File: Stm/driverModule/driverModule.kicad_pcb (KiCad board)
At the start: 4 copper layers, 111.9 x 61.1 mm, 62 parts, among them J1 1723104104, J2 2041119-1 (Mini Pcie Express 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, J3 1723103105, J4 353180420, J5 1723103105, Q1 BSS138, Q2 BSS138, Q3 AON7410, U1 TLE94103EP, U102 ADM7171ACPZ-3.0-R7, U103 TJA1051T-3, U104 TPS5410DR, U2 74LVC2G04, U201 DRV8838, U204 VNH5019A-E, U3 MCP2003B-E/SN

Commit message: routing
Finished PCB routing
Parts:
- added 12V: TestPoint_Small, TestPoint:TestPoint_Pad_1.0x1.0mm, F.Cu at (183.0, 111.6)
- added 3V3: TestPoint_Small, TestPoint:TestPoint_Pad_1.0x1.0mm, F.Cu at (210.7, 64.8)
- added 5V: TestPoint_Small, TestPoint:TestPoint_Pad_1.0x1.0mm, F.Cu at (206.5, 91.2)
- added MISO: TestPoint_Small, TestPoint:TestPoint_Pad_1.0x1.0mm, F.Cu at (149.1, 75.6)
- added MOSI: TestPoint_Small, TestPoint:TestPoint_Pad_1.0x1.0mm, F.Cu at (146.9, 75.6)
- added cs: TestPoint_Small, TestPoint:TestPoint_Pad_1.0x1.0mm, F.Cu at (151.5, 75.6)
- added sck: TestPoint_Small, TestPoint:TestPoint_Pad_1.0x1.0mm, F.Cu at (161.1, 82.8)
- moved J4 22.0 mm to (200.5, 79.7), turned to 90 degrees
- moved R3 14.3 mm to (168.7, 79.0)
- moved Q2 14.3 mm to (171.4, 79.0)
- moved R4 14.3 mm to (174.4, 79.6)
- moved C102 14.0 mm to (206.1, 101.0), turned to 180 degrees
- moved C103 13.9 mm to (208.7, 101.0)
- moved C106 13.8 mm to (185.2, 108.3), turned to 90 degrees
- moved C101 13.6 mm to (207.0, 94.6)
- moved U102 13.6 mm to (207.2, 97.7)
- moved Q1 13.0 mm to (171.5, 85.0)
- moved R1 13.0 mm to (168.7, 84.9)
- moved R101 12.8 mm to (186.1, 96.3)
- moved U104 12.8 mm to (187.0, 101.9)
- moved C104 12.8 mm to (190.9, 107.3)
- moved C105 12.8 mm to (189.1, 93.2)
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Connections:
- J2 pad 1: /CPU Board Connector/+5V -> +5V
- J2 pad 3: /CPU Board Connector/+5V -> +5V
- J2 pad 5: /CPU Board Connector/+5V -> +5V
- J3 pad 4: /Harness/LatchMotorB -> /Harness/LatchMotorA
- J3 pad 5: /Harness/LatchMotorA -> /Harness/LatchMotorB
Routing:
- net +12V: track 0.00 -> 252.2 mm, vias 0 -> 11
- net +5V: track 0.00 -> 163.1 mm, vias 0 -> 2
- net /Harness/WindowMotorB: track 0.00 -> 91.2 mm, vias 0 -> 2
- net /LatchSensorGreenConnector: track 0.00 -> 77.6 mm
- net /LatchSensorPurpleConnector: track 0.00 -> 72.4 mm
- net /Harness/WindowMotorA: track 0.00 -> 64.5 mm, vias 0 -> 2
- net /LatchPositionThroughSignal: track 0.00 -> 56.1 mm, vias 0 -> 2
- net GND: track 0.00 -> 49.3 mm, vias 0 -> 47
- net /Harness/MirrorMotorXYB: track 0.00 -> 46.3 mm
- net /WindowMotorEnable: track 0.00 -> 44.8 mm, vias 0 -> 3
- net +3V3: track 0.00 -> 42.3 mm, vias 0 -> 11
- net /KeyfobClose3v3: track 0.00 -> 42.3 mm, vias 0 -> 2
- net /Harness/MirrorMotorXA: track 0.00 -> 40.5 mm
- net /CAN_RX: track 0.00 -> 40.0 mm, vias 0 -> 2
- net /Harness/keyFobOpen12V: track 0.00 -> 37.0 mm
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- added copper zone on B.Cu, net +12V
- added copper zone on F.Cu, net +12V
- added copper zone on In2.Cu, net +3V3
- added copper zone on F.Cu, net +5V
- added copper zone on F.Cu, net /Motors Interface/Vout
- added copper zone on F.Cu, net /Power/PH
- added copper zone on F.Cu, net GND
- added copper zone on In1.Cu, net GND
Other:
- board size 111.9 x 61.1 mm -> 100.6 x 64.1 mm

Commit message: routing
Update board routing
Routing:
- net +5V: track 163.1 -> 158.7 mm
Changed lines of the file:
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@@
 		(attr smd)
 		(fp_line
+			(start 14.96 -26.81)
+			(end 14.96 -4.2291)
+			(stroke
+				(width 0.1)
+				(type default)
+			)
+			(layer "F.SilkS")
+		)
+		(fp_line
+			(start -15.04 -26.81)
+			(end 14.96 -26.81)
+			(stroke
+				(width 0.1)
+				(type default)
+			)
+			(layer "F.SilkS")
+		)
+		(fp_line
 			(start 15.0749 -4.2291)
 			(end 10.862937 -4.2291)
@@
 		)
 		(fp_line
+			(start -15.04 0)
+			(end -15.04 -26.81)
+			(stroke
+				(width 0.1)
+				(type default)
+			)
+			(layer "F.SilkS")
+		)
+		(fp_line
 			(start 15.0749 1.46846)
 			(end 15.0749 -4.2291)
@@
 			(layer "B.SilkS")
 		)
+		(fp_circle
+			(center 12.1 -23.88)
+			(end 13.4 -23.88)
+			(stroke
+				(width 0.1)
+				(type solid)
+			)
+			(fill no)
+			(layer "Edge.Cuts")
+		)
+		(fp_circle
+			(center -12.1 -23.88)
+			(end -10.8 -23.88)
+			(stroke
+				(width 0.1)
+				(type solid)
+			)
+			(fill no)
+			(layer "Edge.Cuts")
+		)
 		(fp_line
 			(start 16.580396 -5.408201)
@@
 		(model "${KICAD_USER_3D_MODELS_DIR}/2041119-1.stp"
 			(offset
-				(xyz 0 4 2)
+				(xyz 0 4.5 2)
 			)
 			(scale
@@
 	)
 	(gr_rect
-		(start 117.1 79.42)
-		(end 137.81 109.63)
-		(stroke
-			(width 0.1)
-			(type default)
-		)
-		(fill no)
-		(layer "F.SilkS")
-	)
-	(gr_rect
 		(start 114.2 53.1)
 		(end 214.8 117.19)
@@
 	)
 	(segment
-		(start 206.8 95.4)
-		(end 206.484999 95.4)
-		(width 0.15)
+		(start 118.1 78.57)
+		(end 119.4 79.87)
+		(width 0.5)
 		(layer "F.Cu")
 		(net 2)
 	)
 	(segment
-		(start 189.145 95.95)
-		(end 191.55 95.95)
+		(start 131.56 87.93)
+		(end 131.56 96.66)
 		(width 0.5)
 		(layer "F.Cu")
@@
 	)
 	(segment
-		(start 122 60.4)
-		(end 118.1 64.3)
+		(start 206.8 95.4)
+		(end 206.484999 95.4)
+		(width 0.15)
+		(layer "F.Cu")
+		(net 2)
+	)
+	(segment
+		(start 189.145 95.95)
+		(end 191.55 95.95)
 		(width 0.5)
 		(layer "F.Cu")
@@
 	)
 	(segment
+		(start 119.4 79.87)
+		(end 123.5 79.87)
+		(width 0.5)
+		(layer "F.Cu")
+		(net 2)
+	)
+	(segment
 		(start 206.985 96.2522)
 		(end 206.985 95.585)
@@
 	)
 	(segment
-		(start 139.5 98.4)
-		(end 143.46 102.36)
+		(start 133.3 98.4)
+		(end 139.5 98.4)
 		(width 0.5)
 		(layer "F.Cu")
@@
 	)
 	(segment
-		(start 121.8 98.4)
-		(end 139.5 98.4)
-		(width 0.5)
-		(layer "F.Cu")
-		(net 2)
-	)
-	(segment
-		(start 118.1 64.3)
-		(end 118.1 94.7)
+		(start 124.445 60.4)
+		(end 122 60.4)
 		(width 0.5)
 		(layer "F.Cu")
@@
 	)
 	(segment
-		(start 124.445 60.4)
-		(end 122 60.4)
+		(start 118.1 64.3)
+		(end 118.1 78.57)
 		(width 0.5)
 		(layer "F.Cu")
@@
 	)
 	(segment
-		(start 118.1 94.7)
-		(end 121.8 98.4)
+		(start 123.5 79.87)
+		(end 131.56 87.93)
 		(width 0.5)
 		(layer "F.Cu")
@@
 		(layer "F.Cu")
 		(net 2)
+	)
+	(segment
+		(start 139.5 98.4)
+		(end 143.46 102.36)
+		(width 0.5)
+		(layer "F.Cu")
+		(net 2)
+	)
+	(segment
+		(start 122 60.4)
+		(end 118.1 64.3)
+		(width 0.5)
+		(layer "F.Cu")
+		(net 2)
+	)
+	(segment
+		(start 131.56 96.66)
+		(end 133.3 98.4)
+		(width 0.5)
+		(layer "F.Cu")
+		(net 2)

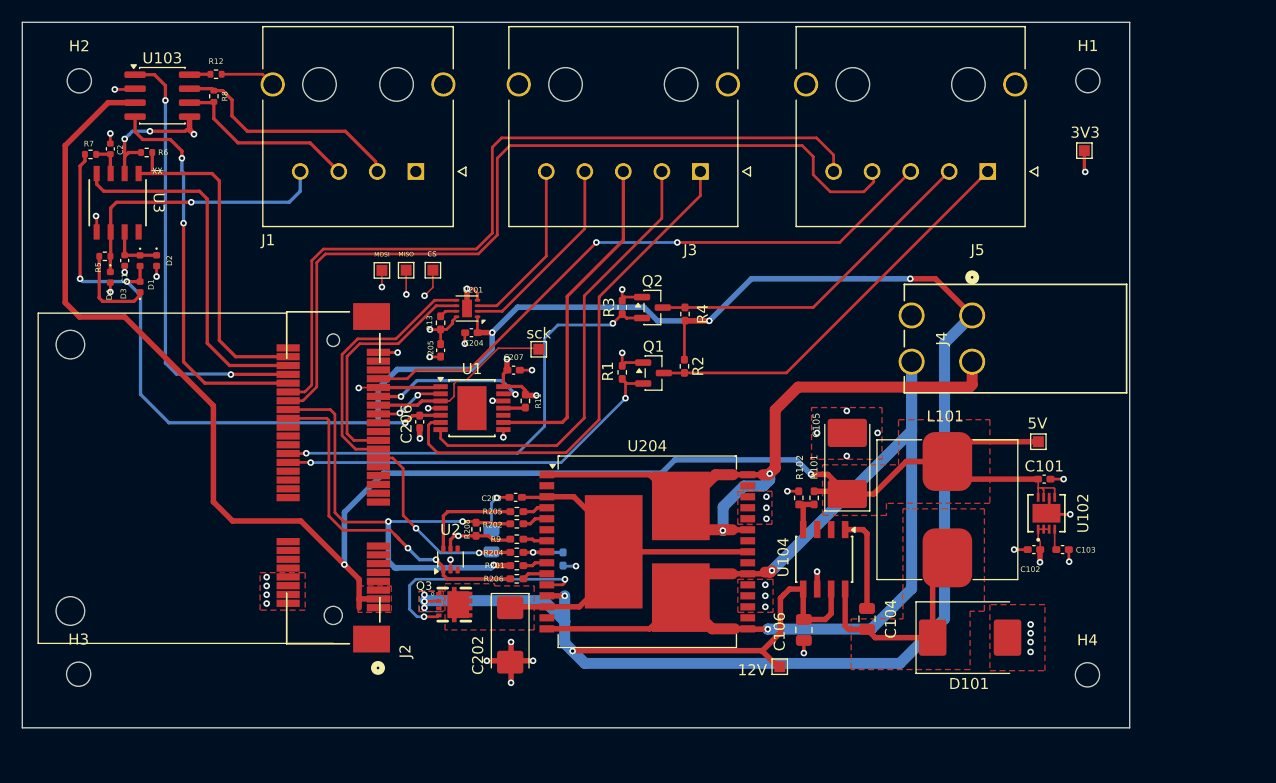
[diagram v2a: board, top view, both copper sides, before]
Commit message: ADC
Added adc to read passenger input signals
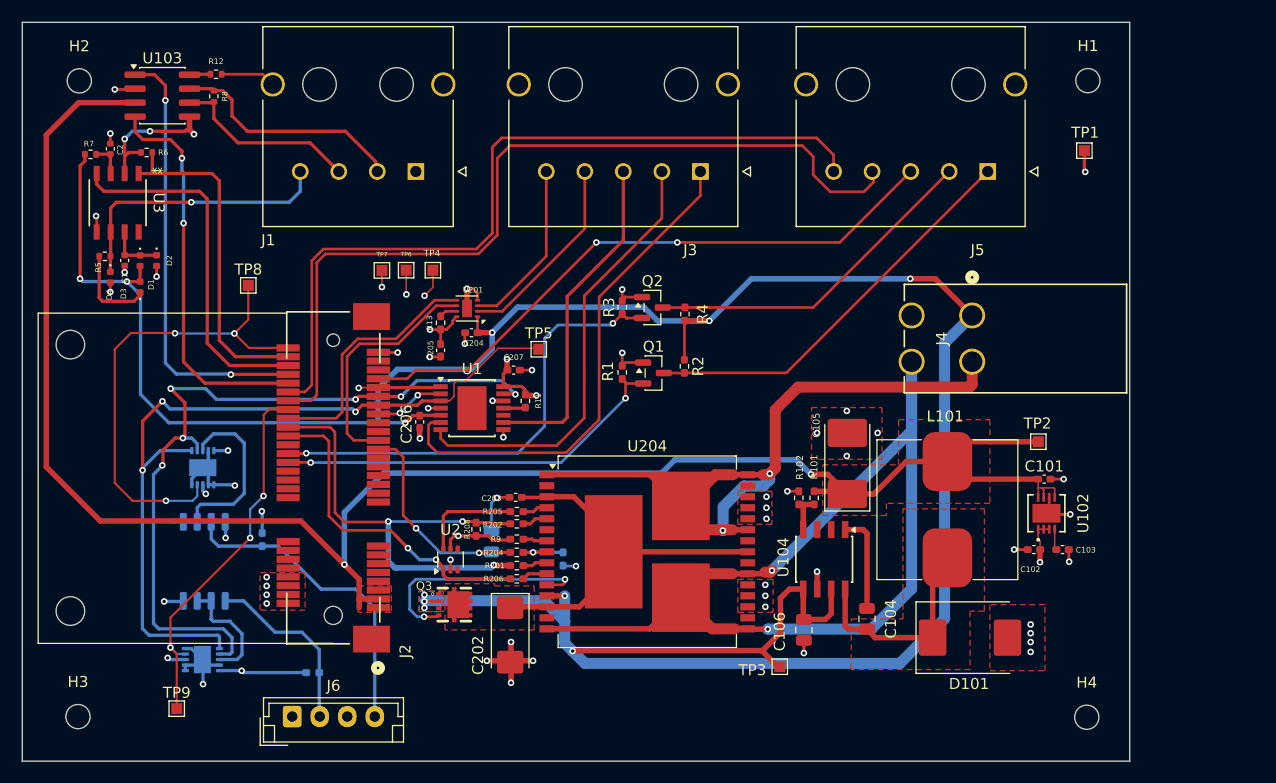
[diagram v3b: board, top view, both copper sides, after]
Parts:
- added J6: Conn_01x04, Connector_JST:JST_EH_B4B-EH-A_1x04_P2.50mm_Vertical, F.Cu at (138.7, 116.2)
- added R10: R_US, Resistor_SMD:R_0402_1005Metric_Pad0.72x0.64mm_HandSolder, B.Cu at (136.0, 100.1)
- added R14: R_US, Resistor_SMD:R_0402_1005Metric_Pad0.72x0.64mm_HandSolder, B.Cu at (140.6, 112.2)
- added TP8: TestPoint_Small, TestPoint:TestPoint_Pad_1.0x1.0mm, F.Cu at (134.7, 77.0)
- added TP9: TestPoint_Small, TestPoint:TestPoint_Pad_1.0x1.0mm, F.Cu at (128.2, 115.5)
- added U4: AD7171, Package_DFN_QFN:DFN-10-1EP_3x3mm_P0.5mm_EP1.55x2.48mm, B.Cu at (130.6, 111.0)
- added U5: AD7171, Package_DFN_QFN:DFN-10-1EP_3x3mm_P0.5mm_EP1.55x2.48mm, B.Cu at (130.6, 93.6)
- added U6: AD8629ARZ-REEL, Package_SO:SOIC-8_5.3x5.3mm_P1.27mm, B.Cu at (130.7, 102.1)
- moved H4 3.85 mm to (210.9, 116.2)
- moved H3 3.85 mm to (119.3, 116.2)
- renumbered 3V3 to TP1, 5V to TP2, 12V to TP3, cs to TP4, sck to TP5, MISO to TP6, MOSI to TP7
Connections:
- J2 pad 27: /WindowMotorCurrentSense -> unconnected-(J2-Pad27)
- J2 pad 29: /LatchMotorEnable -> /WindowMotorCurrentSense
- J2 pad 32: unconnected-(J2-Pad32) -> /WindowMotorDir
- J2 pad 34: unconnected-(J2-Pad34) -> /WindowMotorEnable
- J2 pad 36: /WindowMotorDir -> /LatchMotorEnable
- J2 pad 38: /WindowMotorEnable -> /~{pdrst2}
- J2 pad 52: unconnected-(J2-Pad52) -> /~{pdrst1}
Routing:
- net /SpiClock: track 17.4 -> 72.8 mm, vias 0 -> 3
- net /SpiMasterInput: track 26.4 -> 81.7 mm, vias 3 -> 7
- net /~{pdrst1}: track 0.00 -> 43.4 mm, vias 0 -> 3
- net /~{pdrst2}: track 0.00 -> 34.4 mm, vias 0 -> 3
- net /AD7171/V1: track 0.00 -> 28.9 mm
- net GND: track 49.3 -> 66.9 mm, vias 47 -> 50
- net /AD7171/ain1+: track 0.00 -> 17.0 mm
- net /AD7171/V2: track 0.00 -> 16.5 mm
- net +3V3: track 42.3 -> 58.0 mm, vias 11 -> 17
- net /AD7171/ain2+: track 0.00 -> 10.5 mm
- net +5V: track 158.7 -> 166.3 mm
- net /WindowMotorDir: track 32.2 -> 30.4 mm
- net /WindowMotorEnable: track 44.8 -> 43.2 mm
- net /WindowMotorCurrentSense: track 19.2 -> 20.2 mm
- net /LatchMotorEnable: track 23.6 -> 22.8 mm
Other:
- board size 100.6 x 64.1 mm -> 100.6 x 67.1 mm

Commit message: Capacitors
Added some filter capacitors
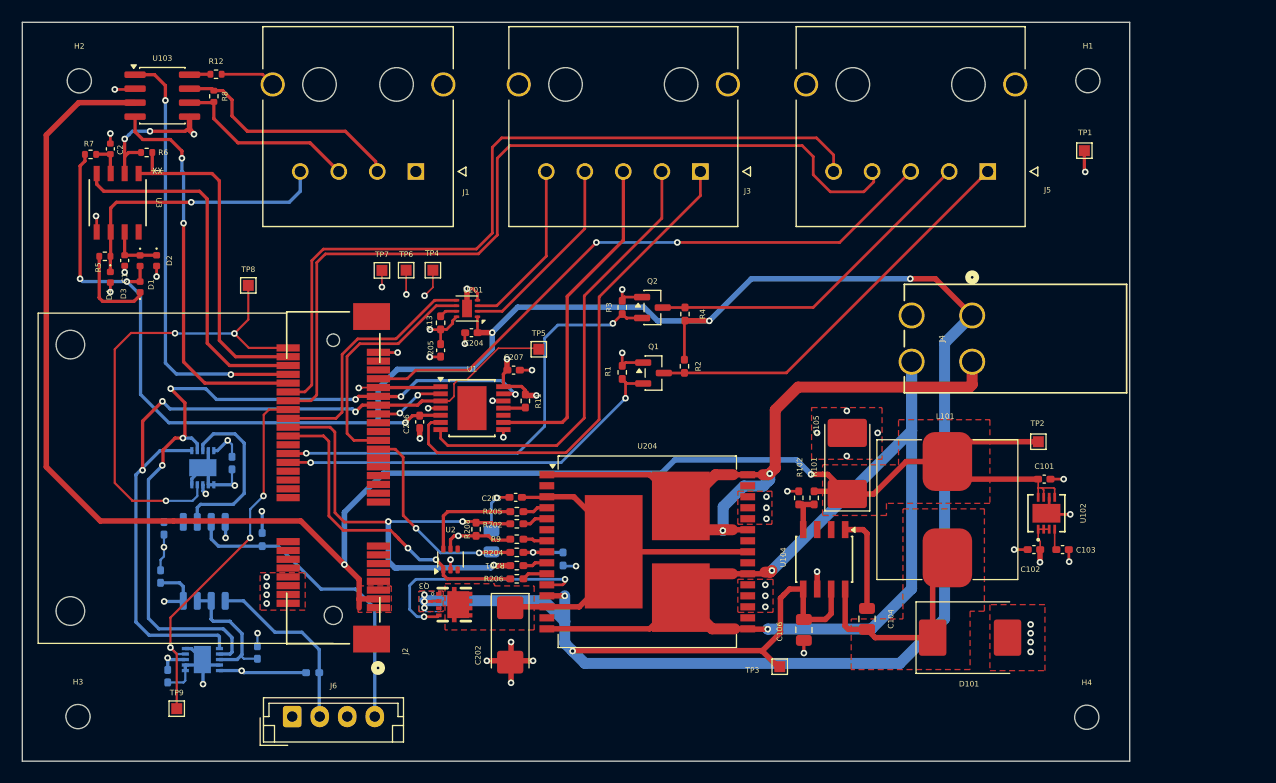
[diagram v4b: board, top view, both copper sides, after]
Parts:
- added C3: 0u1, Capacitor_SMD:C_0402_1005Metric_Pad0.74x0.62mm_HandSolder, B.Cu at (133.2, 93.1)
- added C4: 0u1, Capacitor_SMD:C_0402_1005Metric_Pad0.74x0.62mm_HandSolder, B.Cu at (126.8, 103.5)
- added C5: 0u1, Capacitor_SMD:C_0402_1005Metric_Pad0.74x0.62mm_HandSolder, B.Cu at (127.4, 112.5)
- added C6: 1u, Capacitor_SMD:C_0402_1005Metric_Pad0.74x0.62mm_HandSolder, B.Cu at (135.6, 110.3)
- added C7: 1u, Capacitor_SMD:C_0402_1005Metric_Pad0.74x0.62mm_HandSolder, B.Cu at (127.1, 99.1)
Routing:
- net GND: track 66.9 -> 75.7 mm, vias 50 -> 52
- net +3V3: track 58.0 -> 64.6 mm
- net /AD7171/ain1+: track 17.0 -> 18.8 mm
- net /AD7171/ain2+: track 10.5 -> 12.1 mm

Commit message: Small modifications
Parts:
- added TP10: TestPoint_Small, TestPoint:TestPoint_Pad_1.0x1.0mm, F.Cu at (166.8, 91.0)
- moved R11 11.4 mm to (152.2, 95.9), turned to 180 degrees
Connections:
- R11 pad 2: /Motors Interface/Enable -> /MirrorSpiChipSelect
- U2 pad 3: unconnected-(U2-Pad3) -> /MirrorSpiChipSelect
- U2 pad 4: unconnected-(U2-Pad4) -> /Motors Interface/Enable
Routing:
- net /Motors Interface/Enable: track 2.02 -> 38.7 mm, vias 0 -> 4
- net /MirrorSpiChipSelect: track 18.5 -> 37.5 mm, vias 3 -> 5
- net +3V3: track 64.6 -> 62.0 mm
- net /WindowMotorEnable: track 43.2 -> 44.2 mm
